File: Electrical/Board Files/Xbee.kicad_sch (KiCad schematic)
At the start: 5 parts, among them U7 XBP9B-DMWTB002

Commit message: Adding some device footprints and MPN
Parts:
- C33, C34: MANUFACTURER (none) -> CL10A105KB8NNNC
- C35: MANUFACTURER (none) -> CL10A106MA8NRNC
- R21: footprint (none) -> Resistor_SMD:R_0603_1608Metric
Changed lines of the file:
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@@
     (property "Reference" "R21" (id 0) (at 143.51 55.88 90))
     (property "Value" "10k" (id 1) (at 143.51 58.42 90))
-    (property "Footprint" "" (id 2) (at 143.256 61.214 90)
+    (property "Footprint" "Resistor_SMD:R_0603_1608Metric" (id 2) (at 143.256 61.214 90)
       (effects (font (size 1.27 1.27)) hide)
     )
@@
       (effects (font (size 1.27 1.27)) hide)
     )
+    (property "MANUFACTURER" "CL10A106MA8NRNC" (id 4) (at 100.33 82.55 0)
+      (effects (font (size 1.27 1.27)) hide)
+    )
     (pin "1")
     (pin "2")
@@
     )
     (property "Datasheet" "~" (id 3) (at 94.234 82.55 0)
+      (effects (font (size 1.27 1.27)) hide)
+    )
+    (property "MANUFACTURER" "CL10A105KB8NNNC" (id 4) (at 94.234 82.55 0)
       (effects (font (size 1.27 1.27)) hide)
     )
@@
       (effects (font (size 1.27 1.27)) hide)
     )
+    (property "MANUFACTURER" "CL10A105KB8NNNC" (id 4) (at 87.376 82.55 0)
+      (effects (font (size 1.27 1.27)) hide)
+    )

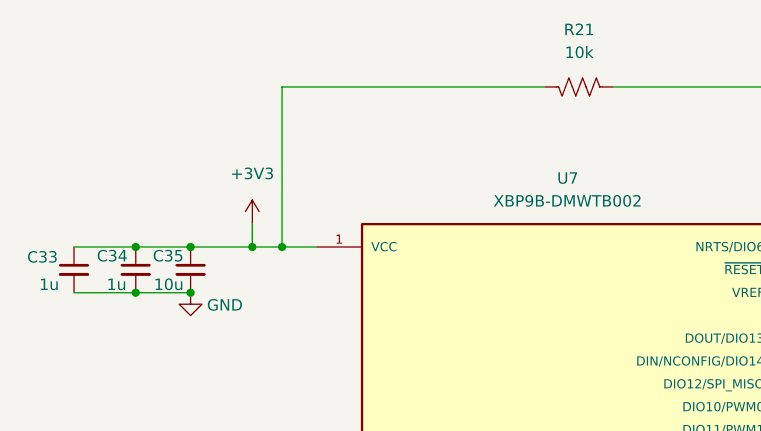
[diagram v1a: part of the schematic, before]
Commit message: Adding footprints
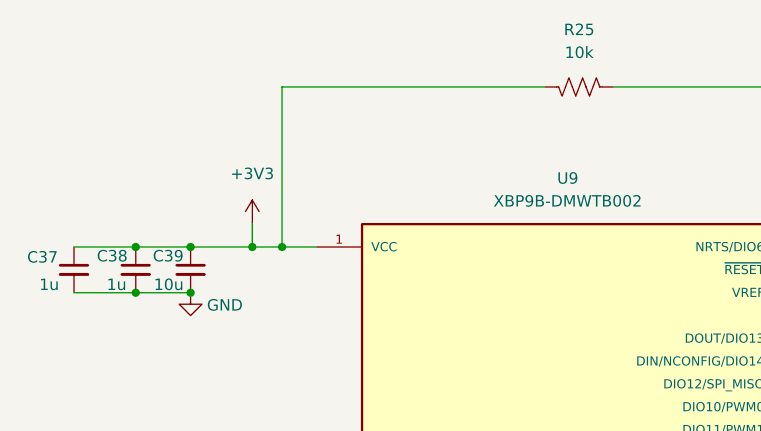
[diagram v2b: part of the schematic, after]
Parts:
- C37: renamed from C33; footprint (none) -> Capacitor_SMD:C_0805_2012Metric
- C38: renamed from C34; footprint (none) -> Capacitor_SMD:C_0805_2012Metric
- C39: renamed from C35; footprint (none) -> Capacitor_SMD:C_0805_2012Metric
- U9: renamed from U7; footprint XBP9-DMWTB002-XBEE-PRO-900HP:DIP2200W51P200L3294H279Q20P -> (none)
- renumbered R21 to R25
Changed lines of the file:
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@@
   (symbol (lib_id "power:+3V3") (at 107.188 77.343 0) (unit 1)
     (in_bom yes) (on_board yes) (fields_autoplaced)
-    (property "Reference" "#PWR040" (id 0) (at 107.188 81.153 0)
+    (property "Reference" "#PWR046" (id 0) (at 107.188 81.153 0)
       (effects (font (size 1.27 1.27)) hide)
     )
@@
   (symbol (lib_id "Device:R_US") (at 143.51 62.23 270) (mirror x) (unit 1)
     (in_bom yes) (on_board yes) (fields_autoplaced)
-    (property "Reference" "R21" (id 0) (at 143.51 55.88 90))
+    (property "Reference" "R25" (id 0) (at 143.51 55.88 90))
     (property "Value" "10k" (id 1) (at 143.51 58.42 90))
     (property "Footprint" "Resistor_SMD:R_0603_1608Metric" (id 2) (at 143.256 61.214 90)
@@
   (symbol (lib_id "Device:C_Small") (at 100.33 82.55 0) (mirror y) (unit 1)
     (in_bom yes) (on_board yes)
-    (property "Reference" "C35" (id 0) (at 99.568 81.026 0)
+    (property "Reference" "C39" (id 0) (at 99.568 81.026 0)
       (effects (font (size 1.27 1.27)) (justify left))
     )
@@
       (effects (font (size 1.27 1.27)) (justify left))
     )
-    (property "Footprint" "" (id 2) (at 100.33 82.55 0)
+    (property "Footprint" "Capacitor_SMD:C_0805_2012Metric" (id 2) (at 100.33 82.55 0)
       (effects (font (size 1.27 1.27)) hide)
     )
@@
   (symbol (lib_id "Device:C_Small") (at 94.234 82.55 0) (mirror y) (unit 1)
     (in_bom yes) (on_board yes)
-    (property "Reference" "C34" (id 0) (at 93.345 81.026 0)
+    (property "Reference" "C38" (id 0) (at 93.345 81.026 0)
       (effects (font (size 1.27 1.27)) (justify left))
     )
@@
       (effects (font (size 1.27 1.27)) (justify left))
     )
-    (property "Footprint" "" (id 2) (at 94.234 82.55 0)
+    (property "Footprint" "Capacitor_SMD:C_0805_2012Metric" (id 2) (at 94.234 82.55 0)
       (effects (font (size 1.27 1.27)) hide)
     )
@@
   (symbol (lib_id "power:GND") (at 100.33 85.09 0) (unit 1)
     (in_bom yes) (on_board yes)
-    (property "Reference" "#PWR039" (id 0) (at 100.33 91.44 0)
+    (property "Reference" "#PWR045" (id 0) (at 100.33 91.44 0)
       (effects (font (size 1.27 1.27)) hide)
     )
@@
   (symbol (lib_id "Device:C_Small") (at 87.376 82.55 0) (mirror y) (unit 1)
     (in_bom yes) (on_board yes)
-    (property "Reference" "C33" (id 0) (at 85.598 81.153 0)
+    (property "Reference" "C37" (id 0) (at 85.598 81.153 0)
       (effects (font (size 1.27 1.27)) (justify left))
     )
@@
       (effects (font (size 1.27 1.27)) (justify left))
     )
-    (property "Footprint" "" (id 2) (at 87.376 82.55 0)
+    (property "Footprint" "Capacitor_SMD:C_0805_2012Metric" (id 2) (at 87.376 82.55 0)
       (effects (font (size 1.27 1.27)) hide)
     )
@@
   (symbol (lib_id "xbp9b-dmwtb002:XBP9B-DMWTB002") (at 142.24 100.33 0) (mirror y) (unit 1)
     (in_bom yes) (on_board yes) (fields_autoplaced)
-    (property "Reference" "U7" (id 0) (at 142.24 72.39 0))
+    (property "Reference" "U9" (id 0) (at 142.24 72.39 0))
     (property "Value" "XBP9B-DMWTB002" (id 1) (at 142.24 74.93 0))
-    (property "Footprint" "XBP9-DMWTB002-XBEE-PRO-900HP:DIP2200W51P200L3294H279Q20P" (id 2) (at 142.24 100.33 0)
+    (property "Footprint" "" (id 2) (at 142.24 100.33 0)
       (effects (font (size 1.27 1.27)) (justify left bottom) hide)
     )
@@
   (symbol (lib_id "power:GND") (at 111.76 123.19 0) (unit 1)
     (in_bom yes) (on_board yes)
-    (property "Reference" "#PWR041" (id 0) (at 111.76 129.54 0)
+    (property "Reference" "#PWR047" (id 0) (at 111.76 129.54 0)
       (effects (font (size 1.27 1.27)) hide)
     )
